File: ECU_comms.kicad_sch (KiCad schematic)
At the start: 21 parts, among them J10 Debug connector, J11 Debug connector, J12 Debug connector, J13 Debug connector, J4 VAN Debug LEDs, Q5 NMOS, Q6 NMOS, U10 NTS0104GU12_115, U3 TSS463C, U4 MCP2551-I-SN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

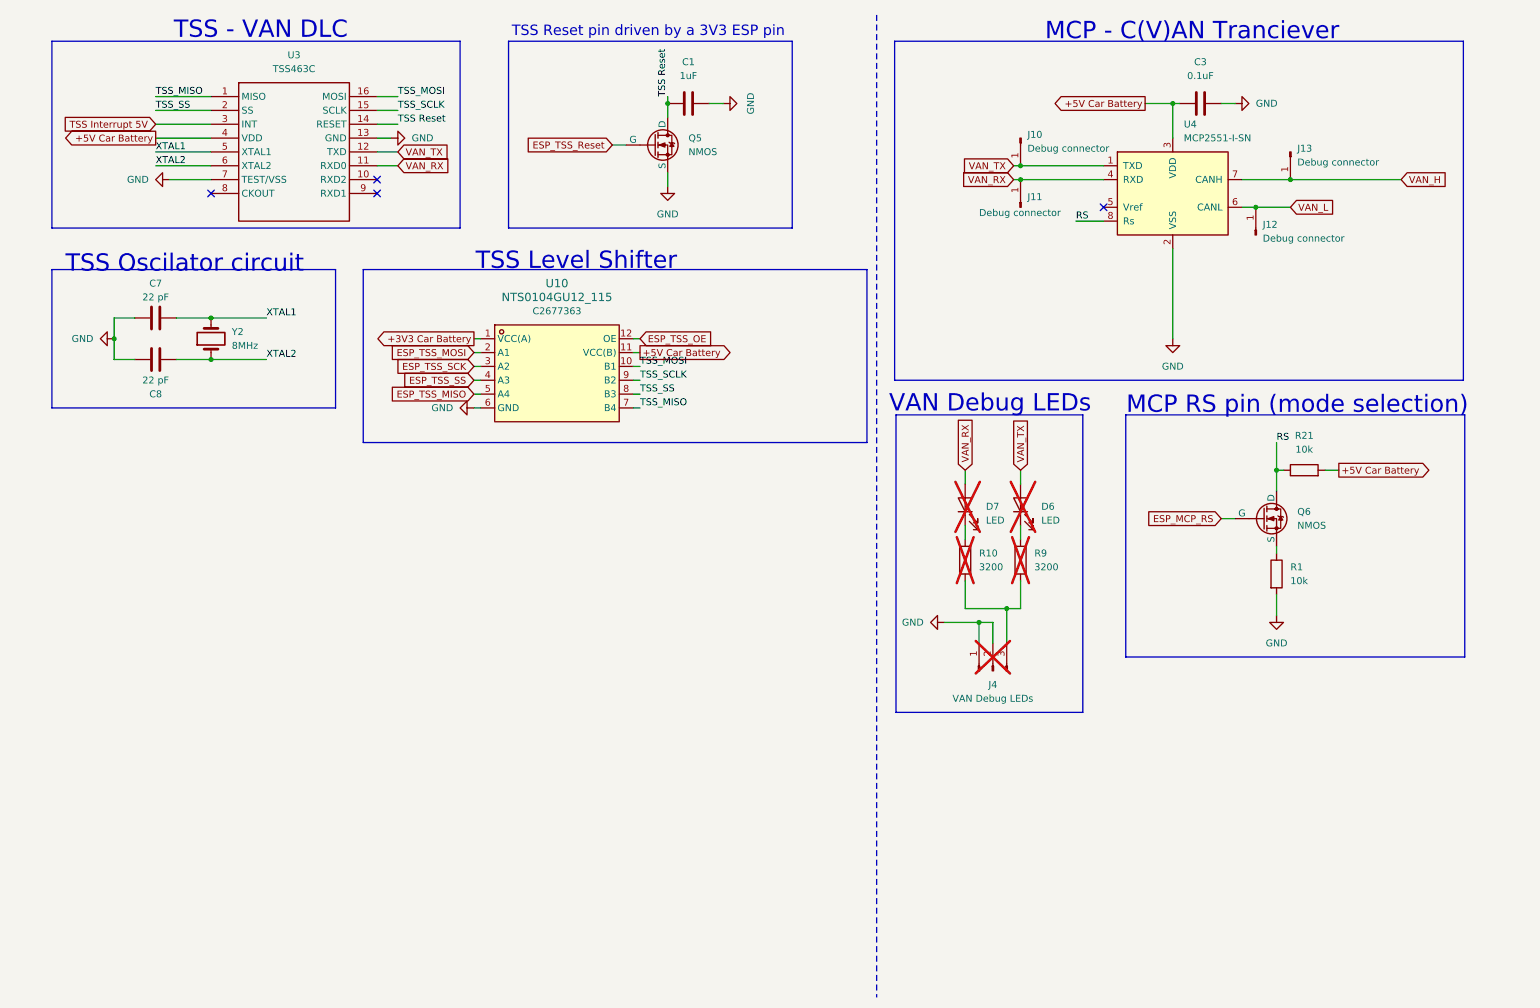
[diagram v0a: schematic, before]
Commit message: implemented the changes from 'Board defects'
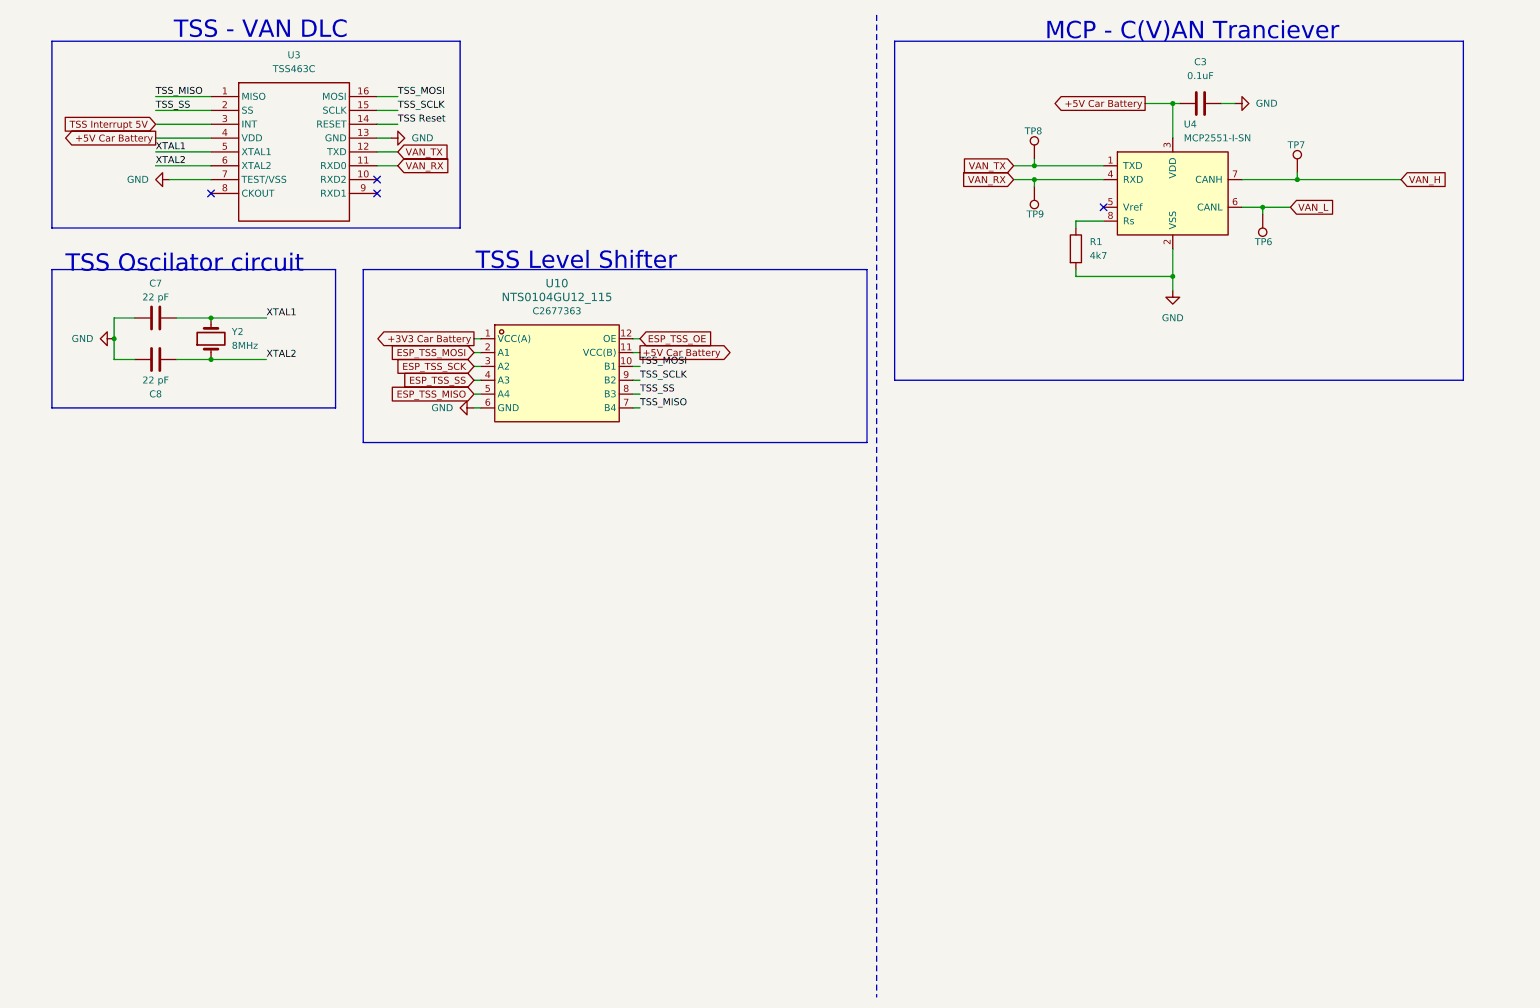
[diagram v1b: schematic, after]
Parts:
- removed C1: 1uF, Capacitor_SMD:C_0805_2012Metric, symbol Device:C
- removed D6, D7: LED, LED_SMD:LED_0402_1005Metric, symbol Device:LED
- removed J10, J11: Debug connector, TestPoint:TestPoint_Loop_D1.80mm_Drill1.0mm_Beaded, symbol Connector:Conn_01x01_Pin
- removed J12, J13: Debug connector, TestPoint:TestPoint_Keystone_5000-5004_Miniature, symbol Connector:Conn_01x01_Pin
- removed J4: VAN Debug LEDs, Connector_PinHeader_2.54mm:PinHeader_1x03_P2.54mm_Vertical, symbol Connector:Conn_01x03_Pin
- removed Q5, Q6: NMOS, Package_TO_SOT_SMD:SOT-723, symbol Simulation_SPICE:NMOS
- removed R10, R9: 3200, Resistor_SMD:R_0805_2012Metric, symbol Device:R
- removed R21: 10k, Resistor_SMD:R_0603_1608Metric_Pad0.98x0.95mm_HandSolder, symbol Device:R
- added TP6, TP7, TP8, TP9: TestPoint, TestPoint:TestPoint_Pad_D1.0mm, symbol Connector:TestPoint
- R1: value 10k -> 4k7; footprint Resistor_SMD:R_0603_1608Metric_Pad0.98x0.95mm_HandSolder -> Resistor_SMD:R_0603_1608Metric
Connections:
- net RS is gone; now on an unnamed net: U4.8 (Rs)
- net VAN_H: now also TP7.1
- net VAN_L: now also TP6.1
- net VAN_RX: now also TP9.1
- net VAN_TX: now also TP8.1
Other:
- note removed: "MCP RS pin (mode selection)"
- note removed: "TSS Reset pin driven by a 3V3 ESP pin"
- note removed: "VAN Debug LEDs"

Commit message: 2 layer PCB
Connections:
- net TSS Interrupt 5V: now also U10.9 (B2)
- net ESP_TSS_SCK renamed TSS Interrupt 3.3V
- net TSS Reset: no longer names the net of U3.14 (RESET)
- net TSS_SCLK renamed TSS_CLK
- net TSS_CLK: no longer U10.9 (B2)
- no-connect marks 4 -> 5

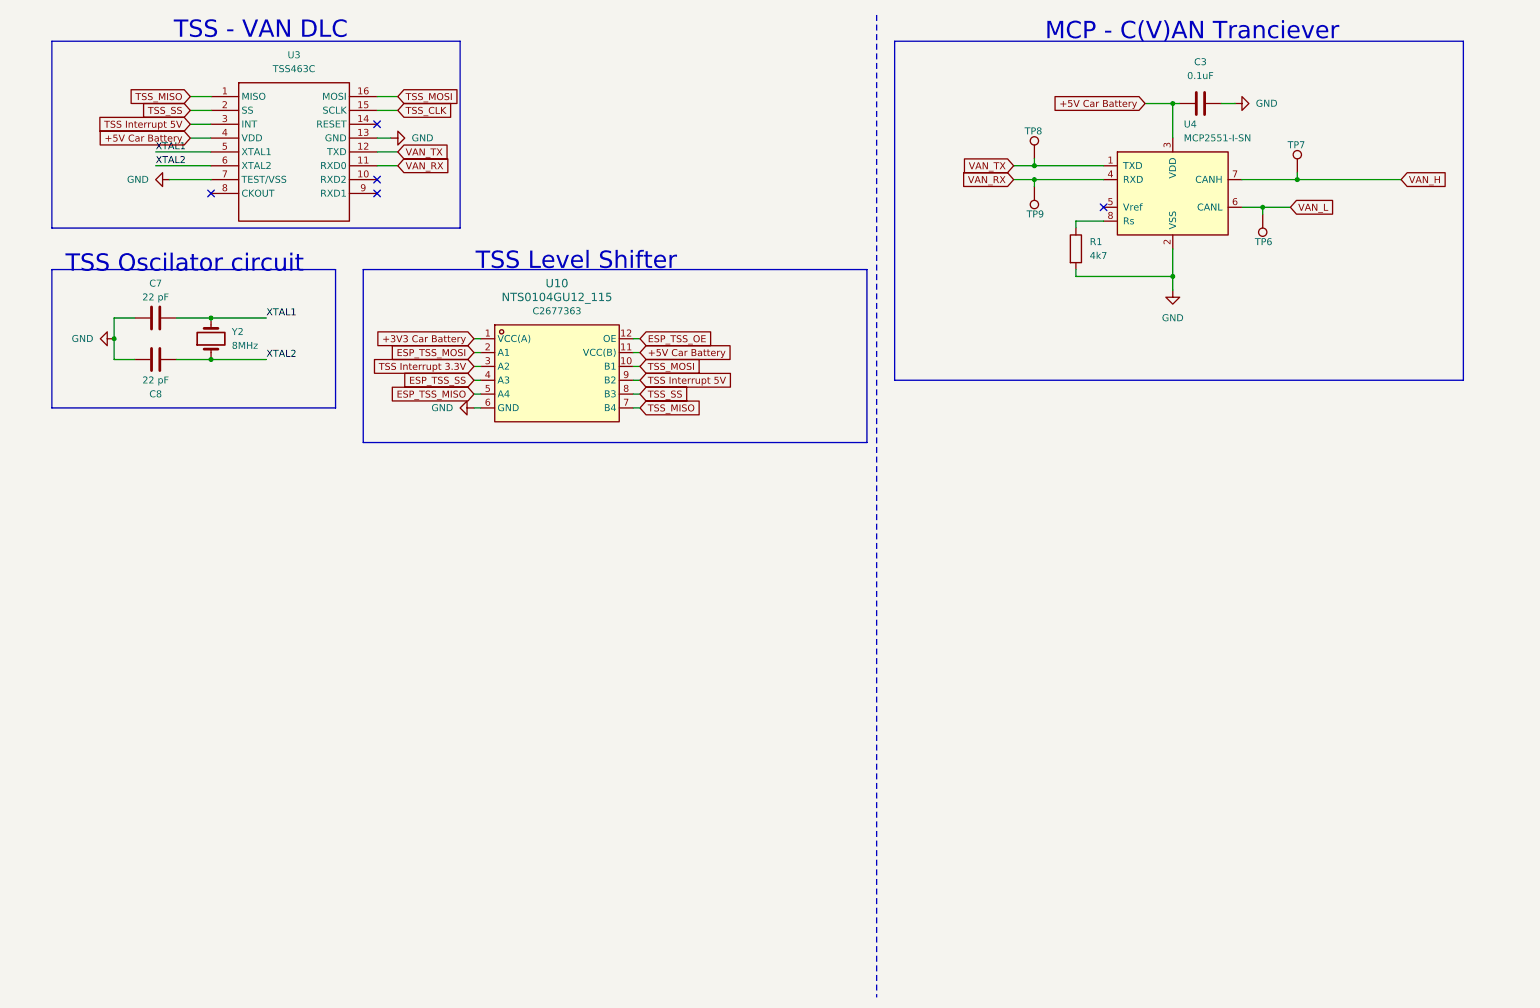
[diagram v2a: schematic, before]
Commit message: changed the CAN transceiever; fixed the transiever typo
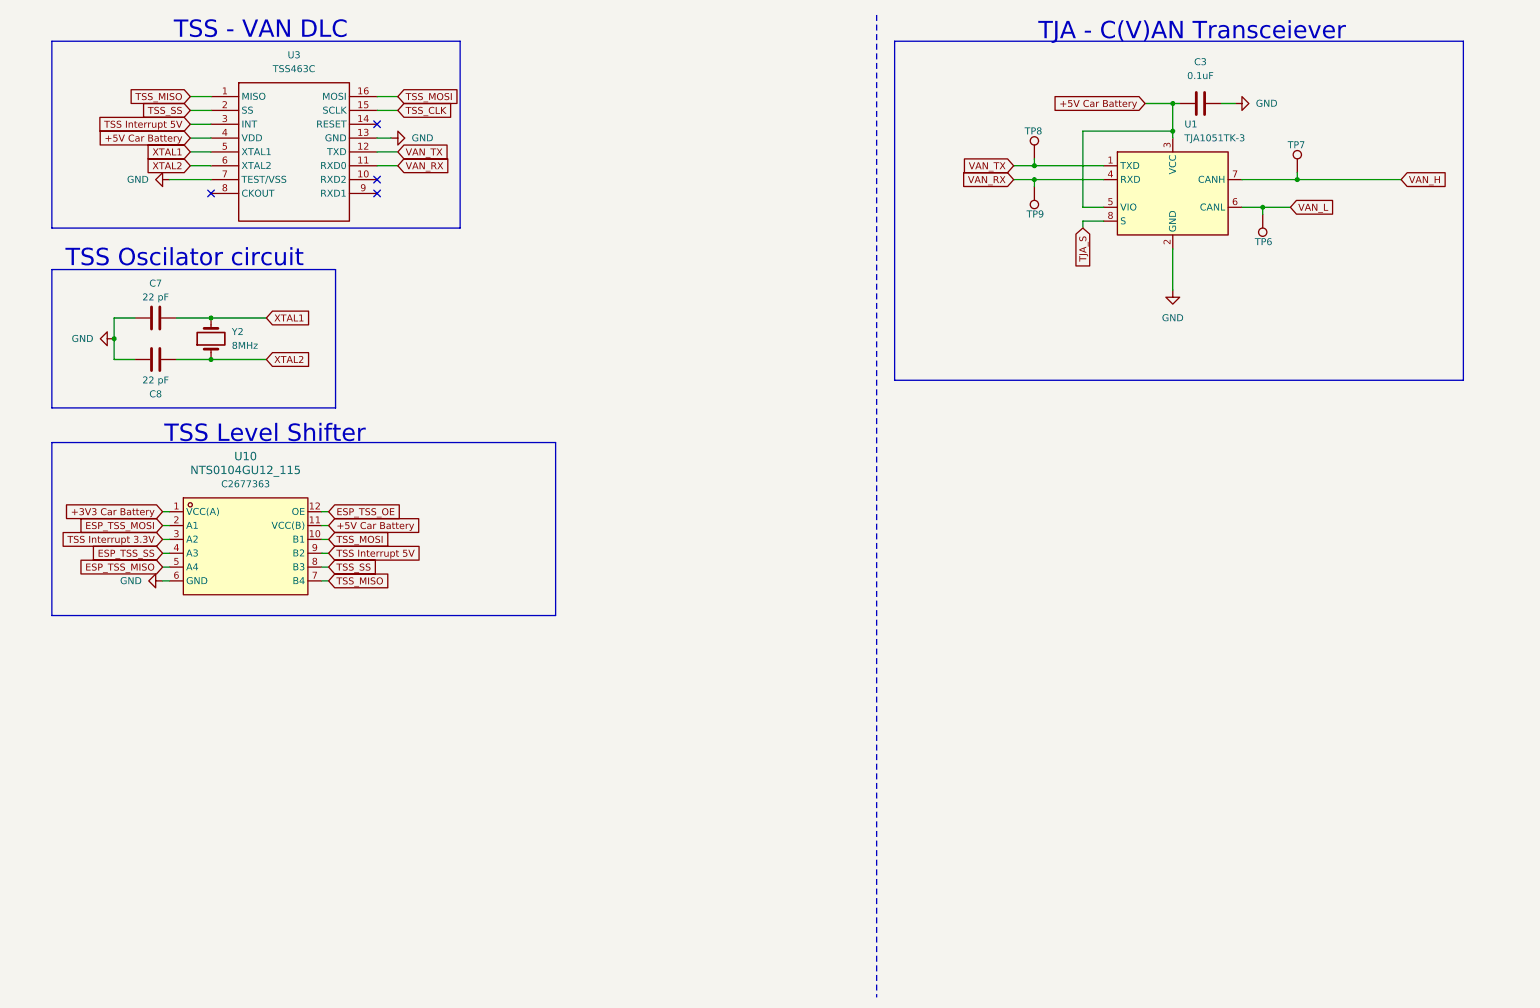
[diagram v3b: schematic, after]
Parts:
- removed R1: 4k7, Resistor_SMD:R_0603_1608Metric, symbol Device:R
- removed U4: MCP2551-I-SN, Package_SO:SOIC-8_3.9x4.9mm_P1.27mm, symbol Interface_CAN_LIN:MCP2551-I-SN
- added U1: TJA1051TK-3, Package_SON:HVSON-8-1EP_3x3mm_P0.65mm_EP1.6x2.4mm, symbol Interface_CAN_LIN:TJA1051TK-3
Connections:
- net +5V Car Battery: now also U1.3 (VCC), U1.5 (VIO)
- net GND: now also U1.2 (GND), U1.9 (GND)
- net VAN_H: now also U1.7 (CANH)
- net VAN_L: now also U1.6 (CANL)
- net VAN_RX: now also U1.4 (RXD)
- net VAN_TX: now also U1.1 (TXD)
- new net TJA_S: U1.8 (S)
- no-connect marks 5 -> 4
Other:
- note added: "TJA - C(V)AN Transceiever"
- note removed: "MCP - C(V)AN Tranciever"
- moved on the sheet: U10

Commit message: changed power regulators, updated PCB
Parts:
- removed Y2: 8MHz, Crystal:Crystal_HC49-4H_Vertical, symbol Device:Crystal
- added U8: ABM3B-8.000MHZ-B2-T, Crystal:Crystal_SMD_EuroQuartz_MJ-4Pin_5.0x3.2mm_HandSoldering, symbol infotainment:ABM3B-8.000MHZ-B2-T
- C7, C8: footprint Capacitor_SMD:C_0402_1005Metric_Pad0.74x0.62mm_HandSolder -> Capacitor_SMD:C_0805_2012Metric
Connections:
- net GND: now also U8.2 (GND), U8.4 (GND)
- net XTAL1: now also U8.1 (XTAL_1)
- net XTAL2: now also U8.3 (XTAL_2)
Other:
- moved on the sheet: C7, C8, U10

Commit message: added 3D models; light touch-ups
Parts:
- removed TP6, TP7, TP8, TP9: TestPoint, TestPoint:TestPoint_Pad_D1.0mm, symbol Connector:TestPoint
- added TP4, TP5: TestPoint, TestPoint:TestPoint_Pad_D1.0mm, symbol Connector:TestPoint
- U8: footprint Crystal:Crystal_SMD_EuroQuartz_MJ-4Pin_5.0x3.2mm_HandSoldering -> Crystal:Crystal_SMD_EuroQuartz_MJ-4Pin_5.0x3.2mm
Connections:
- net VAN_RX: now also TP5.1
- net VAN_TX: now also TP4.1

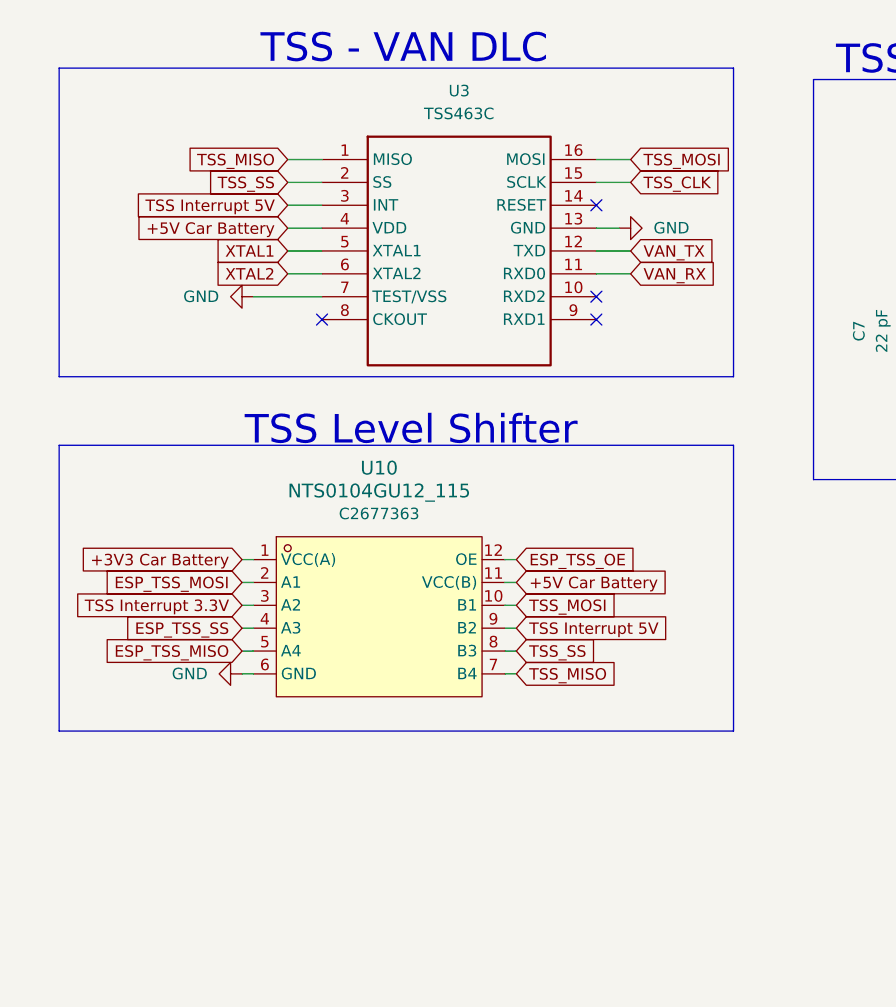
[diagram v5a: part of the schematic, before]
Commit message: added tvs diodes, 100nF, pull-up for TSS interrupt
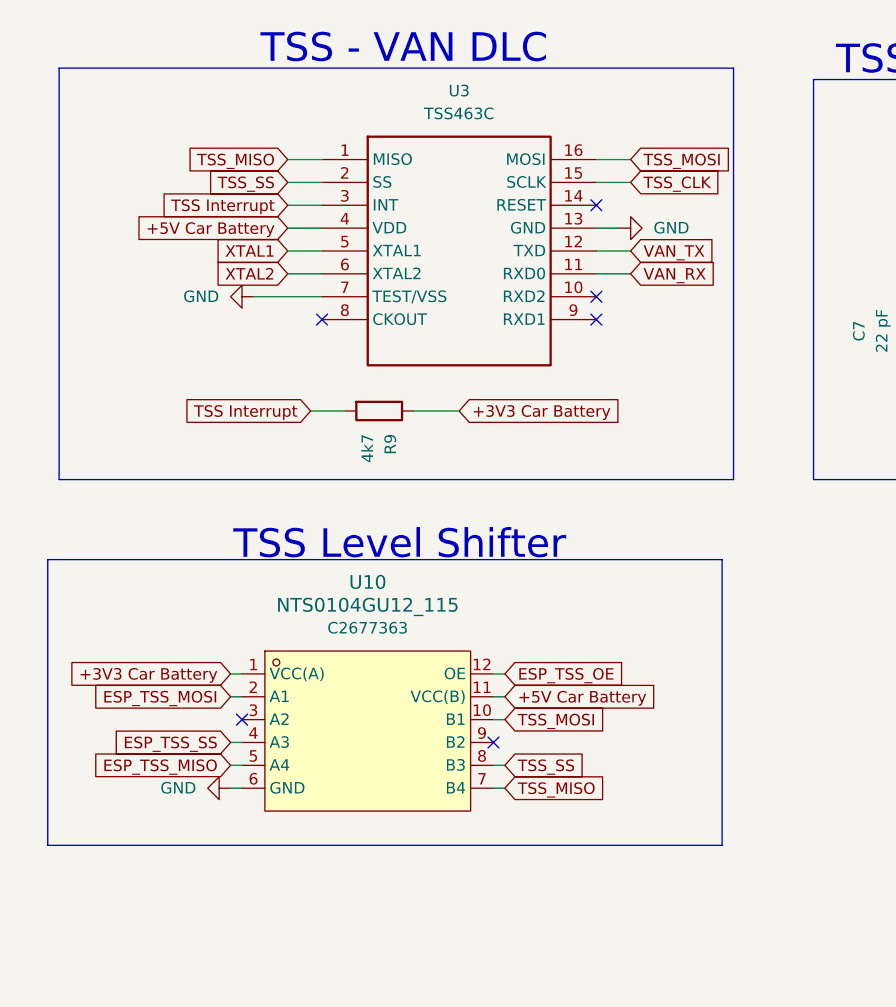
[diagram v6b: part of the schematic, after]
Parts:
- added R9: 4k7, Resistor_SMD:R_0805_2012Metric, symbol Device:R
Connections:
- net +3V3 Car Battery: now also R9.1
- net TSS Interrupt 3.3V: no longer names the net of U10.3 (A2)
- net TSS Interrupt 5V: no longer names the net of U10.9 (B2)
- net TSS Interrupt 5V: no longer U3.3 (INT)
- new net TSS Interrupt: R9.2, U3.3 (INT)
- no-connect marks 4 -> 6
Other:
- moved on the sheet: U10

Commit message: Modified ADC resistors. Added bypass cap to ADC.
Removed some ground islands.
Removed lock files and added them to gitignore.
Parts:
- renumbered TP5 to V_RX1, TP4 to V_TX1
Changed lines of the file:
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@@
 		(on_board yes)
 		(dnp no)
-		(property "Reference" "TP4"
+		(property "Reference" "V_TX1"
 			(at 197.612 35.56 0)
 			(effects
@@
 			(project "main"
 				(path "/3ec17d1d-183f-42c7-9d9d-808fb8c0b5df/1f81d540-bd2e-41ca-a04c-4848f2b3d4b3"
-					(reference "TP4")
+					(reference "V_TX1")
 					(unit 1)
 				)
@@
 		(on_board yes)
 		(dnp no)
-		(property "Reference" "TP5"
+		(property "Reference" "V_RX1"
 			(at 201.422 46.99 0)
 			(effects
@@
 			(project "main"
 				(path "/3ec17d1d-183f-42c7-9d9d-808fb8c0b5df/1f81d540-bd2e-41ca-a04c-4848f2b3d4b3"
-					(reference "TP5")
-					(unit 1)
-				)
+					(reference "V_RX1")
+					(unit 1)
+				)
